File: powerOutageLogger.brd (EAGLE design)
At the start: 127 x 88.9 mm, 38 parts, among them J1 2.1MMJACKTHM, U1 ATmega328P, U2 78L05, U3 DS18B20, Y1 16MHz

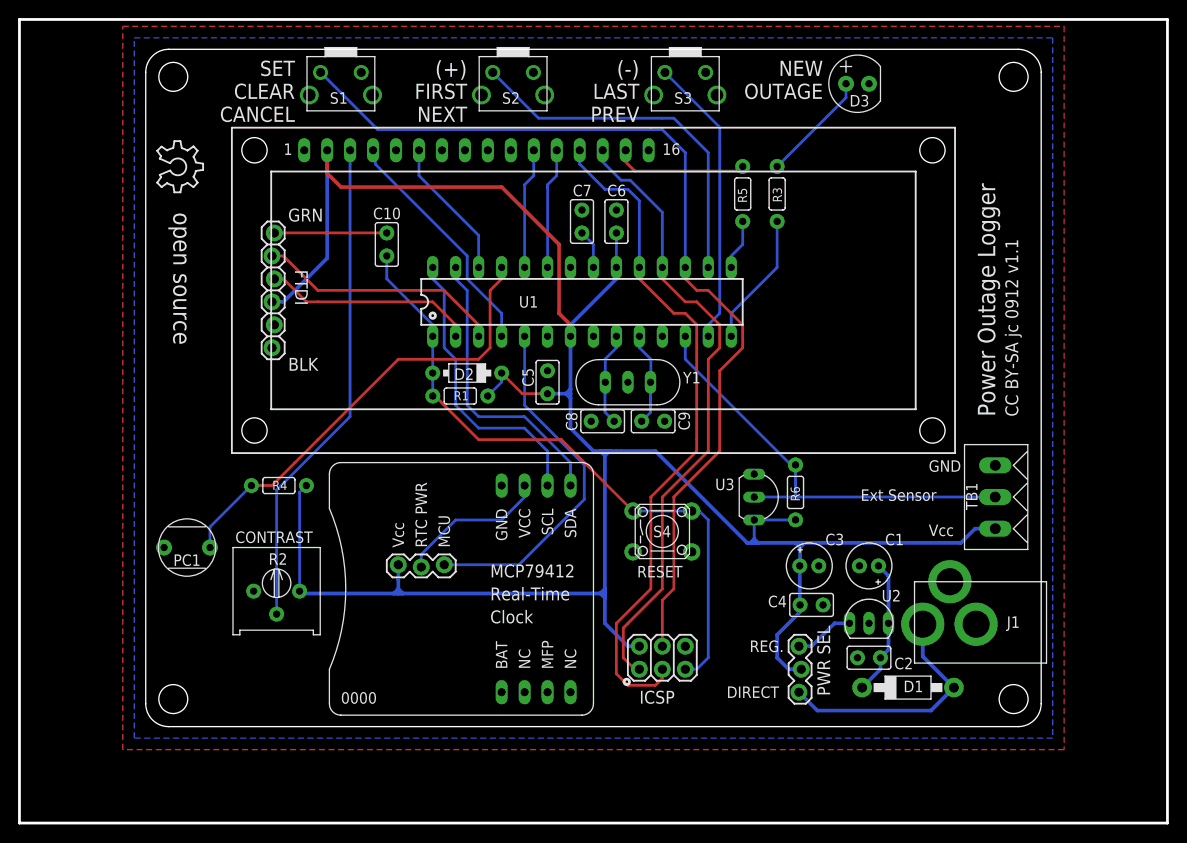
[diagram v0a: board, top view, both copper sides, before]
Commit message: Improved board routing, added connection for RTC interrupt.
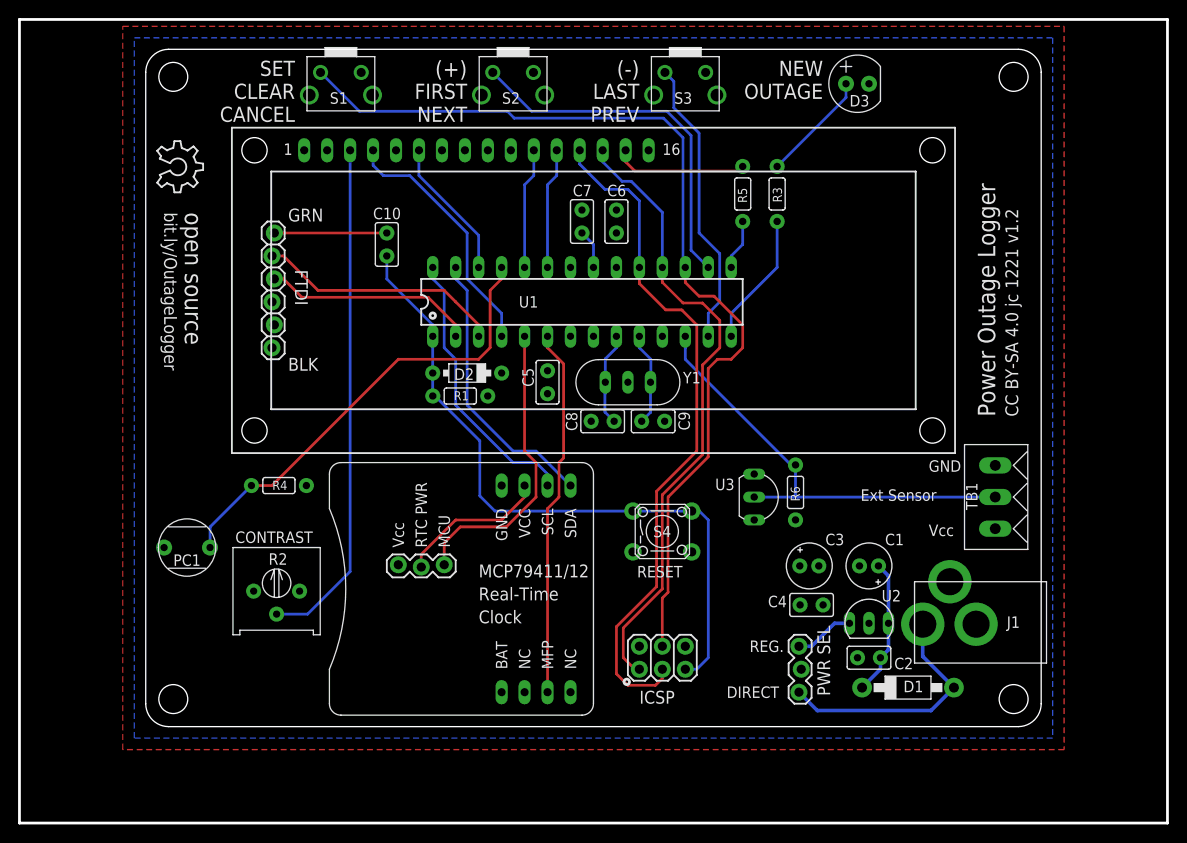
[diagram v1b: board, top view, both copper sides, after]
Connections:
- new net PD4: PCB1.3, U1.6
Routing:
- net VCC: track 262.4 -> 0.00 mm
- net PD4: track 0.00 -> 40.8 mm
- net PD3: track 39.3 -> 33.0 mm
- net /RESET: track 72.1 -> 75.6 mm
- net N$3: track 54.7 -> 56.7 mm
- net MOSI: track 105.7 -> 107.6 mm
- net PD2: track 26.5 -> 28.2 mm
- net SDA: track 32.4 -> 30.9 mm
- net SCL: track 32.4 -> 30.9 mm
- net MISO: track 69.6 -> 70.1 mm
- added copper zone on layer 16, net VCC
- removed copper zone on layer 16, net GND
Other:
- board text added: "CC BY-SA 4.0 jc 1221 v1.2"
- board text added: "MCP79411/12"
- board text added: "bit.ly/OutageLogger"
- board text removed: "0000"
- board text removed: "CC BY-SA jc 0912 v1.1"
- board text removed: "MCP79412"
- board text removed: "http://github.com/JChristensen"
